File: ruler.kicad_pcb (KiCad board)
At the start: 2 copper layers, 170.8 x 38.1 mm, 61 parts, among them J1 USB_OTG, Q1 SOT23, Q2 SOT323, Q3 SOT883, Q4 SOT523, Q5 SOT223, SW1 KMR2, SW2 EVQPE1, SW3 B3U1000P, SW4 FSMCT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

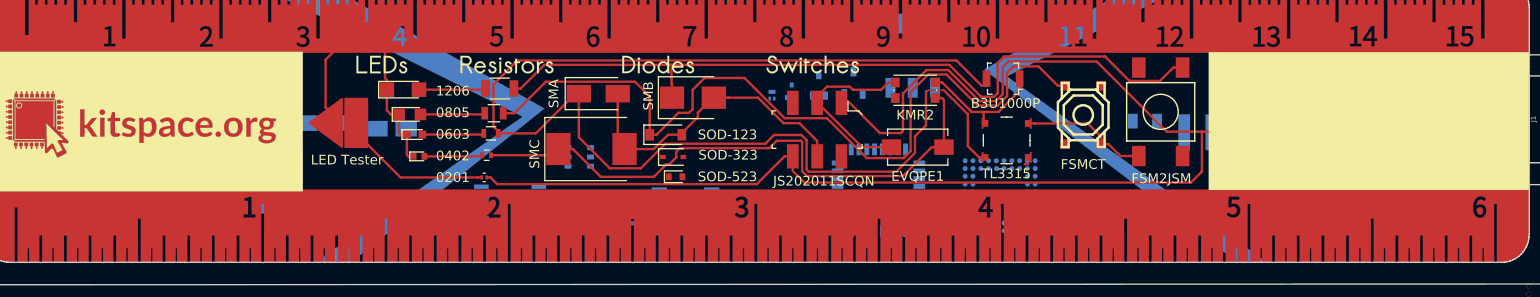
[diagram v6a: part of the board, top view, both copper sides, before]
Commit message: Re-arrange footprints
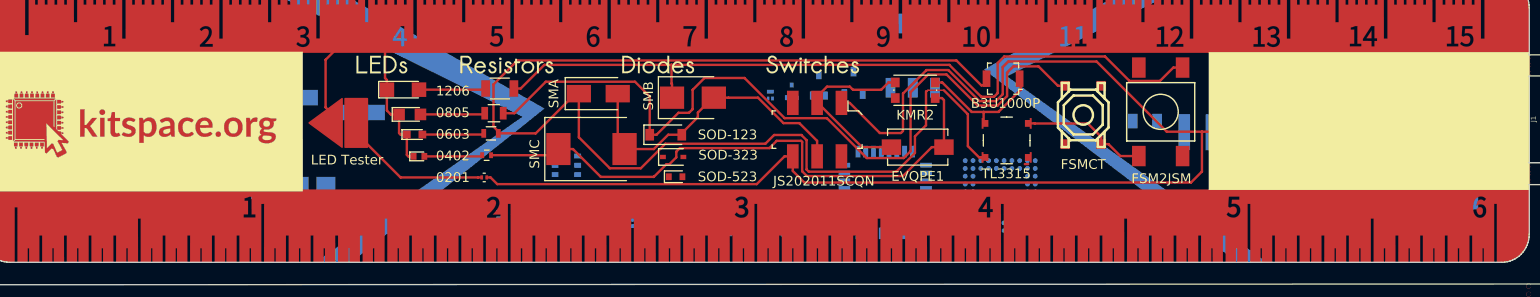
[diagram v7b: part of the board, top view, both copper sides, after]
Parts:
- C4: value 8x5.4mm -> 8x10mm; footprint KiCad/Capacitors_SMD.pretty:CP_Elec_8x5.4 -> KiCad/Capacitors_SMD.pretty:CP_Elec_8x10
- U5: footprint KiCad/Housings_SSOP.pretty:TSSOP-16_4.4x5mm_Pitch0.65mm -> KiCad/Housings_SSOP.pretty:TSSOP-8_3x3mm_Pitch0.65mm
- moved C4 5.24 mm to (78.2, 99.8)
- moved C3 5.18 mm to (88.4, 101.3)
- moved DRAWING9 4.60 mm to (219.7, 108.5)
- moved C2 4.42 mm to (96.8, 102.6)
- moved L2 4.21 mm to (214.3, 112.5)
- moved C1 3.70 mm to (104.1, 104.1)
- moved DRAWING11 3.59 mm to (71.6, 101.1)
- moved L5 2.94 mm to (204.9, 110.1)
- moved C5 2.04 mm to (99.3, 111.5)
- moved U5 1.82 mm to (120.9, 115.3), turned to 180 degrees
- moved L4 1.61 mm to (197.6, 108.1)
- moved U7 1.58 mm to (125.4, 109.6)
- moved C6 1.54 mm to (92.5, 111.8)
- moved U3 1.45 mm to (139.0, 114.7), turned to 180 degrees
- moved C7 0.80 mm to (84.6, 112.3)
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
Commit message: Add drawings, ants etc
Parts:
- added DRAWING13: Conn_01x01, drawings:mouse_bites, B.Cu at (213.4, 97.3)
- added DRAWING14: Conn_01x01, drawings:mouse, B.Cu at (194.7, 97.6)
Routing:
- net GND: track 142.2 -> 35.9 mm
